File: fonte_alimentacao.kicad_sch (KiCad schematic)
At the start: 1 part, among them J1 Conn_01x03

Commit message: Definicao subbass e filtro passa baixo
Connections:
- net +15V renamed +V
- net -15V renamed -V

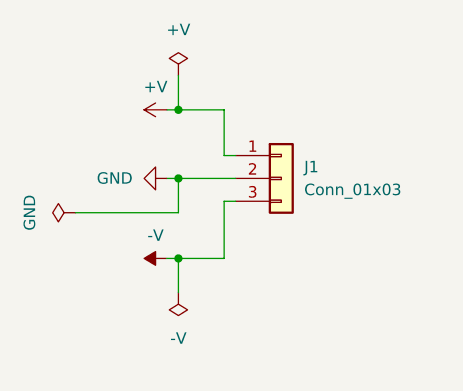
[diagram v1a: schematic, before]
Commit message: Valida cascata subbass 40 Hz e subsonico 10 Hz em ±15 V
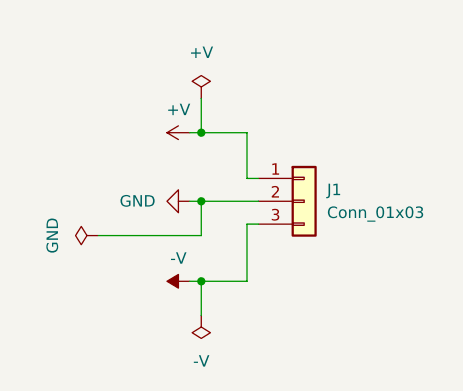
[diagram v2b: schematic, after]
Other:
- moved on the sheet: J1

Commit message: Refactor SubBass project: Update track widths, add new connector symbols, and document modular architecture
- Reduced minimum track width and clearance in hifi_audio.kicad_pro for improved routing.
- Added new connector symbols for AUDIO_IN and AUDIO_OUT in subsbass.kicad_sch.
- Updated footprints for various components in subsbass.kicad_sch to ensure compatibility.
- Introduced modular architecture documentation in arquitetura_modular.md outlining the design and electrical interfaces.
- Created build_subbass_module_board.py script to automate PCB placement from schematic netlist.
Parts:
- J1: footprint (none) -> Connector_JST:JST_XH_B3B-XH-A_1x03_P2.50mm_Vertical
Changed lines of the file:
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@@
 			)
 		)
-		(property "Footprint" ""
+		(property "Footprint" "Connector_JST:JST_XH_B3B-XH-A_1x03_P2.50mm_Vertical"
 			(at 149.86 97.79 0)
 			(hide yes)
